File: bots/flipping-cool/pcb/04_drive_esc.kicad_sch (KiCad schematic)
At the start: 7 parts, among them J20 WEKA_POWER_INPUT_XT30, J21 WEKA_PWM_INPUTS_NAMED, J22 WEKA_MOTOR_OUTPUT_SOLDER_PADS, J23 MOTOR_FRONT_LEFT_POLOLU_3064, J24 MOTOR_REAR_LEFT_POLOLU_3064, J25 MOTOR_FRONT_RIGHT_POLOLU_3064, J26 MOTOR_REAR_RIGHT_POLOLU_3064

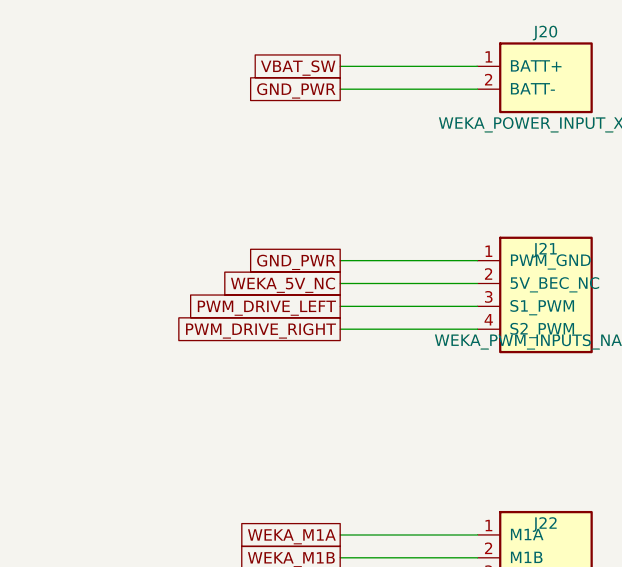
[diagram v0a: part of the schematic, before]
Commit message: Refactor Flipping Cool PCB design to Rev B, updating title, date, and revision details. Integrate ESP32-S3 module and enhance documentation for MCU I/O and debugging features, while maintaining historical context from Rev A.
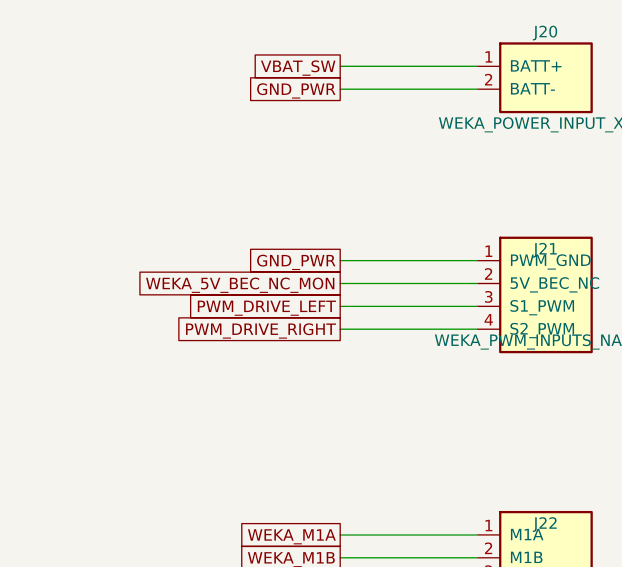
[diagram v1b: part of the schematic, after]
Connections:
- net WEKA_5V_NC renamed WEKA_5V_BEC_NC_MON
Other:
- title: Flipping Cool Rev A - Drive ESC -> Flipping Cool Rev B - Drive ESC and Motors

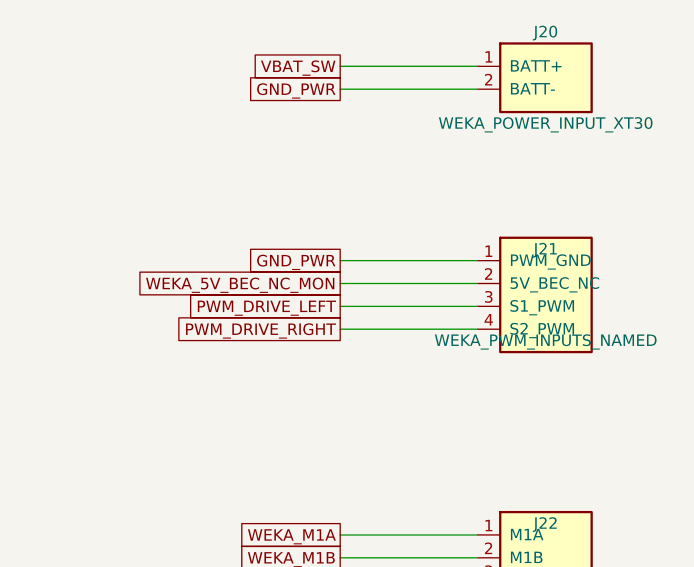
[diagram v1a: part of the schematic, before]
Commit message: Remove obsolete Flipping Cool Rev B project plan file and update schematic files to reflect the latest design changes, including integration of the ESP32-S3 module and enhancements to power management and control authority. Ensure all documentation is aligned with the current PCB design and architecture.
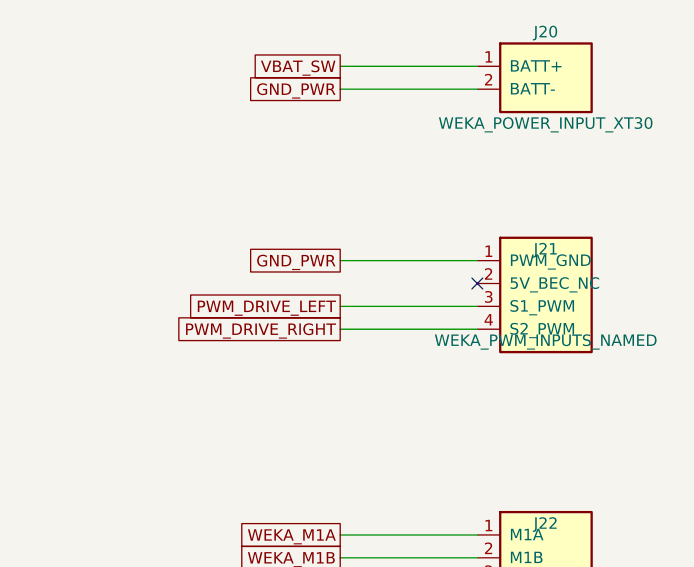
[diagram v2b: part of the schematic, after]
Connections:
- net WEKA_5V_BEC_NC_MON: no longer names the net of J21.2 (5V_BEC_NC)
- no-connect marks 0 -> 1
